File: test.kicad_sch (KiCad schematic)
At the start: 35 parts, among them IC1 USBLC6-2SC6, IC2 ESP32-S3-WROOM-1-N16, J1 PWM, J2 UART0, SW1 Reset, SW2 Button, U1 USB-TYPE-C-018, U2 ADC08351CILQX{slash}NOPB, U3 ADC08351CILQX{slash}NOPB

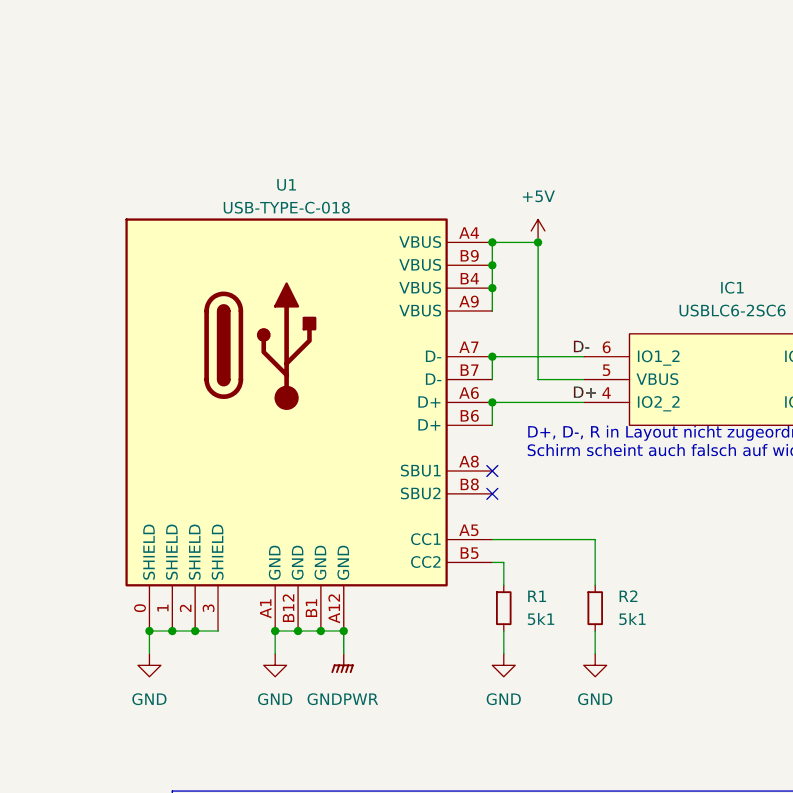
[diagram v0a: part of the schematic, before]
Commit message: new idear to arange gnd ref in layout
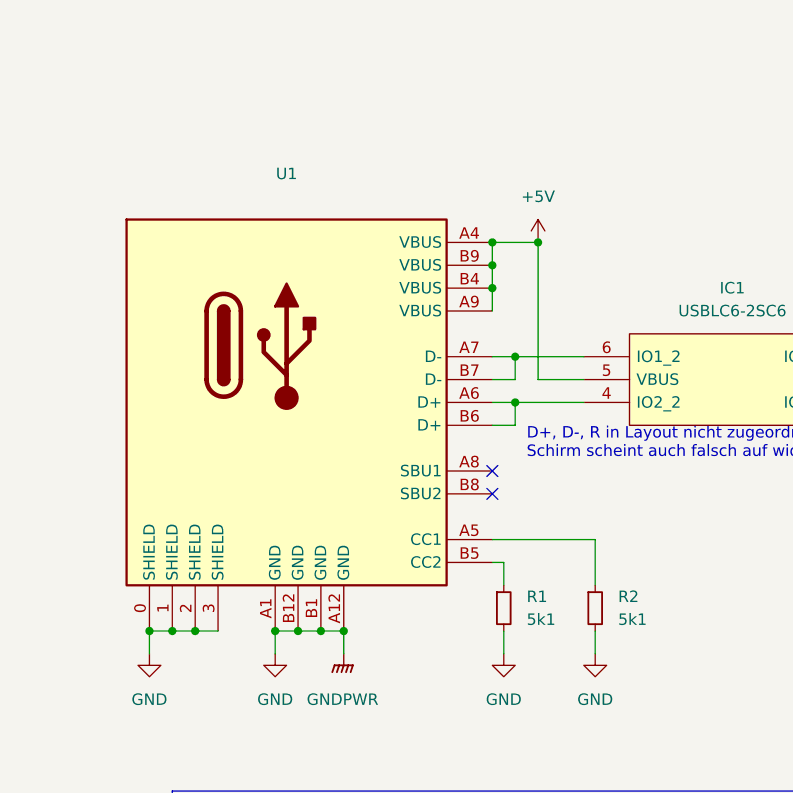
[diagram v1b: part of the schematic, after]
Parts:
- U1: value USB-TYPE-C-018 -> (none); footprint footprint:USB-C_SMD-TYPE-C-31-M-12 -> (none)
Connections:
- net D+: no longer names the net of IC1.4 (IO2_2), U1.A6 (D+), U1.B6 (D+)
- net D-: no longer names the net of IC1.6 (IO1_2), U1.A7 (D-), U1.B7 (D-)

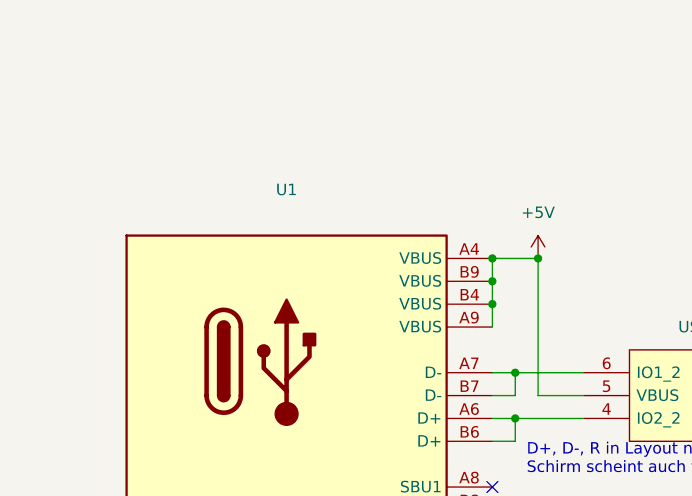
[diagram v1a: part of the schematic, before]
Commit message: added values for analog front end
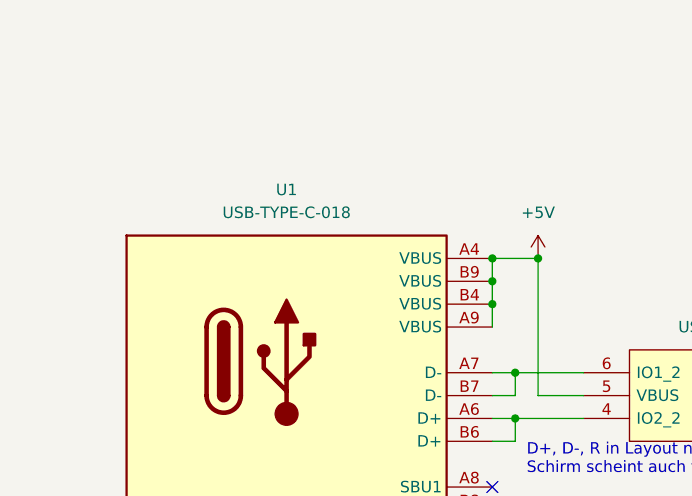
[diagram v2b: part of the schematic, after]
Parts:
- U1: value (none) -> USB-TYPE-C-018; footprint (none) -> project_library:USB-TYPE-C-018

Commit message: new adc
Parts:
- added IC?: AD9288BSTZ-40, project_library:QFP50P900X900X160-48N-AD9288, symbol project_library:AD9288BSTZ-40
- added U?: ESP32-WROOM-E, Espressif:ESP32-WROOM-32E, symbol Espressif:ESP32-WROOM-E
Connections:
- new net: U?.1 (GND), U?.15 (GND), U?.38 (GND)
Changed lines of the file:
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@@
     (pin "1")
+  )
+  (symbol (lib_id "Espressif:ESP32-WROOM-E") (at 415.29 59.69 0) (unit 1)
+    (in_bom yes) (on_board yes) (fields_autoplaced)
+    (property "Reference" "U?" (id 0) (at 415.29 21.59 0))
+    (property "Value" "ESP32-WROOM-E" (id 1) (at 415.29 24.13 0))
+    (property "Footprint" "Espressif:ESP32-WROOM-32E" (id 2) (at 415.29 97.79 0)
+      (effects (font (size 1.27 1.27)) hide)
+    )
+    (property "Datasheet" "https://www.espressif.com/sites/default/files/documentation/esp32-wroom-32e_esp32-wroom-32ue_datasheet_en.pdf" (id 3) (at 415.29 95.25 0)
+      (effects (font (size 1.27 1.27)) hide)
+    )
+    (pin "1")
+    (pin "10")
+    (pin "11")
+    (pin "12")
+    (pin "13")
+    (pin "14")
+    (pin "15")
+    (pin "16")
+    (pin "17")
+    (pin "18")
+    (pin "19")
+    (pin "2")
+    (pin "20")
+    (pin "21")
+    (pin "22")
+    (pin "23")
+    (pin "24")
+    (pin "25")
+    (pin "26")
+    (pin "27")
+    (pin "28")
+    (pin "29")
+    (pin "3")
+    (pin "30")
+    (pin "31")
+    (pin "32")
+    (pin "33")
+    (pin "34")
+    (pin "35")
+    (pin "36")
+    (pin "37")
+    (pin "38")
+    (pin "39")
+    (pin "4")
+    (pin "5")
+    (pin "6")
+    (pin "7")
+    (pin "8")
+    (pin "9")
   )
   (symbol (lib_id "project_library:Button") (at 111.76 38.1 90) (unit 1)
@@
     )
   )
+  (symbol (lib_id "project_library:AD9288BSTZ-40") (at 339.09 130.81 0) (unit 1)
+    (in_bom yes) (on_board yes) (fields_autoplaced)
+    (property "Reference" "IC?" (id 0) (at 386.08 124.2312 0))
+    (property "Value" "AD9288BSTZ-40" (id 1) (at 386.08 126.7712 0))
+    (property "Footprint" "project_library:QFP50P900X900X160-48N-AD9288" (id 2) (at 378.46 113.03 0)
+      (effects (font (size 1.27 1.27)) (justify left) hide)
+    )
+    (property "Datasheet" "http://www.analog.com/media/en/technical-documentation/data-sheets/AD9288.pdf" (id 3) (at 378.46 115.57 0)
+      (effects (font (size 1.27 1.27)) (justify left) hide)
+    )
+    (property "Description" "Analog Devices, AD9288BSTZ-40 Analog Devices AD9288BSTZ-40, 8 bit Parallel ADC, Dual Differential Input, 48-Pin LQFP" (id 4) (at 378.46 118.11 0)
+      (effects (font (size 1.27 1.27)) (justify left) hide)
+    )
+    (property "Height" "1.6" (id 5) (at 378.46 120.65 0)
+      (effects (font (size 1.27 1.27)) (justify left) hide)
+    )
+    (property "Mouser Part Number" "584-AD9288BSTZ-40" (id 6) (at 378.46 123.19 0)
+      (effects (font (size 1.27 1.27)) (justify left) hide)
+    )
+    (property "Mouser Price/Stock" "https://www.mouser.co.uk/ProductDetail/Analog-Devices/AD9288BSTZ-40?qs=%2FtpEQrCGXCxwGu1VSidU0Q%3D%3D" (id 7) (at 378.46 125.73 0)
+      (effects (font (size 1.27 1.27)) (justify left) hide)
+    )
+    (property "Manufacturer_Name" "Analog Devices" (id 8) (at 378.46 128.27 0)
+      (effects (font (size 1.27 1.27)) (justify left) hide)
+    )
+    (property "Manufacturer_Part_Number" "AD9288BSTZ-40" (id 9) (at 378.46 130.81 0)
+      (effects (font (size 1.27 1.27)) (justify left) hide)
+    )
+    (pin "1")
+    (pin "10")
+    (pin "11")
+    (pin "12")
+    (pin "13")
+    (pin "14")
+    (pin "15")
+    (pin "16")
+    (pin "17")
+    (pin "18")
+    (pin "19")
+    (pin "2")
+    (pin "20")
+    (pin "21")
+    (pin "22")
+    (pin "23")
+    (pin "24")
+    (pin "25")
+    (pin "26")
+    (pin "27")
+    (pin "28")
+    (pin "29")
+    (pin "3")
+    (pin "30")
+    (pin "31")
+    (pin "32")
+    (pin "33")
+    (pin "34")
+    (pin "35")
+    (pin "36")
+    (pin "37")
+    (pin "38")
+    (pin "39")
+    (pin "4")
+    (pin "40")
+    (pin "41")
+    (pin "42")
+    (pin "43")
+    (pin "44")
+    (pin "45")
+    (pin "46")
+    (pin "47")
+    (pin "48")
+    (pin "5")
+    (pin "6")
+    (pin "7")
+    (pin "8")
+    (pin "9")
+  )
   (symbol (lib_id "power:+3.3V") (at 247.65 50.8 0) (unit 1)
     (in_bom yes) (on_board yes) (fields_autoplaced)
@@
       (reference "IC10") (unit 1) (value "DAC5571IDBVR") (footprint "project_library:DAC5571IDBVR")
     )
+    (path "/f319d031-f112-4b08-a205-7d9414f5c3bf"
+      (reference "IC?") (unit 1) (value "AD9288BSTZ-40") (footprint "project_library:QFP50P900X900X160-48N-AD9288")
+    )
     (path "/ff062df5-8115-40ac-9e51-b96c9808f42d"
       (reference "J1") (unit 1) (value "PWM") (footprint "project_library:725996-2")
@@
       (reference "U10") (unit 3) (value "MCP6022T-I_SN") (footprint "project_library:MCP6022T-I_SN")
     )
-  )
+    (path "/d6fb04dc-8dd4-47e8-aa6e-91850d9215a1"
+      (reference "U?") (unit 1) (value "ESP32-WROOM-E") (footprint "Espressif:ESP32-WROOM-32E")
+    )
+  )

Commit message: changed adc and esp chip
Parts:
- removed C10, C13, C2, C5: 10u, Capacitor_SMD:C_0805_2012Metric_Pad1.18x1.45mm_HandSolder, symbol Device:C_Small
- removed C11, C12, C3, C4, C9: 0.1u, Capacitor_SMD:C_0805_2012Metric_Pad1.18x1.45mm_HandSolder, symbol Device:C_Small
- removed R3: 5k1, Resistor_SMD:R_0805_2012Metric_Pad1.20x1.40mm_HandSolder, symbol Device:R_Small
- removed SW2: Button, project_library:SW_TS-1187A-B-A-B, symbol project_library:Button
- removed U2, U3: ADC08351CILQX/NOPB, project_library:ADC08351CILQX, symbol project_library:ADC08351CILQX{brace}slash}NOPB
- added C? (x9): 0.1u, Capacitor_SMD:C_0805_2012Metric_Pad1.18x1.45mm_HandSolder, symbol Device:C_Small
- added C?: (no value), symbol Device:C_Small
- added Q?: (no value), symbol project_library:SS8050-G
- added Q?: SS8050-G, SOT95P240X115-3N, symbol project_library:SS8050-G
- added R? (x3): (no value), symbol Device:R_Small
- added R? (x2): 10k, Resistor_SMD:R_0805_2012Metric_Pad1.20x1.40mm_HandSolder, symbol Device:R_Small
- added R?: (no value), Resistor_SMD:R_0805_2012Metric_Pad1.20x1.40mm_HandSolder, symbol Device:R_Small
- added SW?: (no value), project_library:SW_TS-1187A-B-A-B, symbol project_library:Button
- added U?: (no value), symbol Interface_USB:CP2102N-Axx-xQFN28
- C6: value 1u -> (none); footprint Capacitor_SMD:C_0805_2012Metric_Pad1.18x1.45mm_HandSolder -> (none)
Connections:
- net +3.3VA: now also IC?.30 (VD_2), IC?.31 (VD_3), IC?.48 (VD_4), C?.1, C?.1
- net +3V3: now also IC?.15 (VDD_1), IC?.28 (VDD_2), IC?.33 (VDD_3), IC?.46 (VDD_4), IC?.8 (S1), IC?.9 (S2), C?.1, C?.1, C?.1, C?.1, C?.1, R?.1, U?.6 (VDD), U?.7 (VREGIN); no longer C1.1
- net +5V: now also R?.1
- net Analog_Out_CH1: now also IC?.2 (AINA)
- net Analog_Out_CH2: now also IC?.11 (AINB)
- net CH1_D0: now also IC?.37 (D0A)
- net CH1_D1: now also IC?.38 (D1A)
- net CH1_D2: now also IC?.39 (D2A)
- net CH1_D3: now also IC?.40 (D3A)
- net CH1_D4: now also IC?.41 (D4A)
- net CH1_D5: now also IC?.42 (D5A)
- net CH1_D6: now also IC?.43 (D6A)
- net CH1_D7: now also IC?.44 (D7A_(MSB))
- net CH2_D0: now also IC?.24 (D0B)
- net CH2_D1: now also IC?.23 (D1B)
- net CH2_D2: now also IC?.22 (D2B)
- net CH2_D3: now also IC?.21 (D3B)
- net CH2_D4: now also IC?.20 (D4B)
- net CH2_D5: now also IC?.19 (D5B)
- net CH2_D6: now also IC?.18 (D6B)
- net CH2_D7: now also IC?.17 ((MSB)_D7B)
- net ENABLE: now also Q?.3; no longer IC2.3 (EN)
- net GND: now also IC?.16 (GND_3), IC?.27 (GND_4), IC?.34 (GND_7), IC?.45 (GND_8), C?.2, C?.2, C?.2, C?.2, C?.2, C?.2, R?.1, R?.2, SW?.A, SW?.B, U?.29 (GND), U?.3 (GND); no longer C1.2
- net I2S_CLK: now also IC?.14 (ENCB), IC?.47 (ENCA)
- net USB_D+: now also U?.4 (D+); no longer IC1.3 (IO2_1), IC2.14 (IO20)
- net USB_D-: now also U?.5 (D-); no longer IC1.1 (IO1_1), IC2.13 (IO19)
- net at U?.34 (U0RXD/GPIO3): now also U?.26 (TXD)
- net at U?.35 (U0TXD/GPIO1): now also U?.25 (RXD)
- net GNDA: now reaches IC?.1 (GND_1)
- net GNDA: now also IC?.29 (GND_5), IC?.32 (GND_6), C?.2, C?.2, C?.2
- net at IC?.12 (GND_2): now also C?.1
- net at IC?.13 (VD_1): now also C?.2
- new net: Q?.1, R?.2 (x2)
- new net: R?.1, U?.11 (~{SUSPEND})
- new net: R?.2, R?.2, U?.8 (VBUS)
- new net: R?.2, U?.9 (~{RST})
- new net DTR: Q?.2, R?.1, U?.28 (~{DTR})
- new net IO0: C?.1, Q?.3, SW?.C, SW?.D
- new net RTS: Q?.2, R?.1, U?.24 (~{RTS})
- no-connect marks 15 -> 24
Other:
- moved on the sheet: C1, C6, C7, C8, SW1

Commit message: updated circuit
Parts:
- removed C1: 0.1u, Capacitor_SMD:C_0805_2012Metric_Pad1.18x1.45mm_HandSolder, symbol Device:C_Small
- removed IC2: ESP32-S3-WROOM-1-N16, project_library:ESP32-S3-WROOM-1, symbol project_library:ESP32-S3-WROOM-1-N16
- removed J2: UART0, Connector_PinHeader_2.54mm:PinHeader_1x04_P2.54mm_Vertical, symbol Connector:Conn_01x04_Male
- removed R4, R5: 6k8, Resistor_SMD:R_0805_2012Metric_Pad1.20x1.40mm_HandSolder, symbol Device:R_Small
- removed R6, R7: 470, Resistor_SMD:R_0805_2012Metric_Pad1.20x1.40mm_HandSolder, symbol Device:R_Small
- removed R8: 1k5, Resistor_SMD:R_0805_2012Metric_Pad1.20x1.40mm_HandSolder, symbol Device:R_Small
- added IC5: TCA9534APWR, project_library:SOP65P640X120-16N, symbol project_library:TCA9534APWR
- added R15: 1k5, Resistor_SMD:R_0805_2012Metric_Pad1.20x1.40mm_HandSolder, symbol Device:R_Small
- added R16, R17: 6k8, Resistor_SMD:R_0805_2012Metric_Pad1.20x1.40mm_HandSolder, symbol Device:R_Small
- added TP4: GNDREF, TestPoint:TestPoint_Keystone_5000-5004_Miniature, symbol Connector:TestPoint
- C10, C11, C12, C2, C3, C5, C9: renamed from C?; footprint Capacitor_SMD:C_0805_2012Metric_Pad1.18x1.45mm_HandSolder -> Capacitor_SMD:C_0603_1608Metric_Pad1.08x0.95mm_HandSolder
- C13: renamed from C?; value (none) -> 0.1u; footprint (none) -> Capacitor_SMD:C_0603_1608Metric_Pad1.08x0.95mm_HandSolder
- C6: value (none) -> 0.1u; footprint (none) -> Capacitor_SMD:C_0805_2012Metric_Pad1.18x1.45mm_HandSolder
- Q1: renamed from Q?; footprint SOT95P240X115-3N -> project_library:SOT95P240X115-3N
- Q2: renamed from Q?; value (none) -> SS8050-G; footprint (none) -> project_library:SOT95P240X115-3N
- R3: renamed from R?; value (none) -> 22.1k; footprint (none) -> Resistor_SMD:R_0805_2012Metric_Pad1.20x1.40mm_HandSolder
- R4: renamed from R?; value (none) -> 47.5k
- R5: renamed from R?; value (none) -> 2k; footprint (none) -> Resistor_SMD:R_0805_2012Metric_Pad1.20x1.40mm_HandSolder
- R6: renamed from R?; value (none) -> 10k; footprint (none) -> Resistor_SMD:R_0805_2012Metric_Pad1.20x1.40mm_HandSolder
- SW2: renamed from SW?; value (none) -> Button
- U2: renamed from U?; value (none) -> CP2102N-A02-GQFN28; footprint (none) -> Package_DFN_QFN:QFN-28-1EP_5x5mm_P0.5mm_EP3.35x3.35mm
- gave numbers to parts that had none: 6
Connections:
- net +3V3: now also IC2.4 (DFS), U3.2 (3V3), IC5.16 (VCC), R16.2, R17.2
- net CH1_AC_Sel: now also IC5.6 (P2)
- net CH1_D0: now also U3.23 (MTDO/GPIO15/ADC2_CH3)
- net CH1_D1: now also U3.14 (MTDI/GPIO12/ADC2_CH5)
- net CH1_D2: now also U3.9 (32K_XN/GPIO33/ADC1_CH5)
- net CH1_D3: now also U3.8 (32K_XP/GPIO32/ADC1_CH4)
- net CH1_D4: now also U3.7 (GPIO35/ADC1_CH7)
- net CH1_D5: now also U3.6 (GPIO34/ADC1_CH6)
- net CH1_D6: now also U3.5 (SENSOR_VN/GPIO39/ADC1_CH3)
- net CH1_D7: now also U3.4 (SENSOR_VP/GPIO36/ADC1_CH0)
- net CH2_AC_Sel: now also IC5.9 (P4)
- net CH2_D0: now also U3.37 (GPIO23)
- net CH2_D1: now also U3.31 (GPIO19)
- net CH2_D2: now also U3.30 (GPIO18)
- net CH2_D3: now also U3.28 (GPIO17)
- net CH2_D4: now also U3.27 (GPIO16)
- net CH2_D5: now also U3.29 (GPIO5)
- net CH2_D6: now also U3.26 (ADC2_CH0/GPIO4)
- net CH2_D7: now also U3.24 (ADC2_CH2/GPIO2)
- net CS_Gain_CH1: now also IC5.7 (P3)
- net CS_Gain_CH2: now also IC5.10 (P5)
- net Charging: now also IC5.11 (P6)
- net ENABLE: now also U3.3 (EN/CHIP_PU)
- net GND: now also U3.1 (GND), U3.15 (GND), U3.38 (GND), U3.39 (GND_THERMAL), IC5.1 (A0), IC5.2 (A1), IC5.3 (A2), IC5.8 (GND)
- net I2S_CLK: now also U3.12 (ADC2_CH7/GPIO27)
- net IO0: now also U3.25 (GPIO0/BOOT/ADC2_CH1)
- net MOSI: now also U3.16 (MTCK/GPIO13/ADC2_CH4)
- net RX: now also U2.25 (RXD), U3.34 (U0RXD/GPIO3)
- net SCLK_SPI: now also U3.13 (MTMS/GPIO14/ADC2_CH6)
- net SCL_I2C: now also U3.36 (GPIO22), IC5.14 (SCL), R16.1
- net SDA: now also U3.33 (GPIO21), IC5.15 (SDA), R17.1
- net Status_PWM: now also IC5.12 (P7), R15.2
- net TX: now also U2.26 (TXD), U3.35 (U0TXD/GPIO1)
- net Trigger_CH1: now also IC5.4 (P0)
- net Trigger_CH2: now also IC5.5 (P1)
- net USB_D+: now also IC1.3 (IO2_1)
- net USB_D-: now also IC1.1 (IO1_1)
- net at D1.2 (A): now also R15.1
- net Offset_CH1: now reaches U3.10 (DAC_1/ADC2_CH8/GPIO25)
- net Offset_CH2: now reaches U3.11 (DAC_2/ADC2_CH9/GPIO26)
- net GNDREF: now reaches IC2.5 (REFINA)
- net GNDREF: now also IC2.6 (REFOUT), IC2.7 (REFINB), TP4.1
- no-connect marks 24 -> 22
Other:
- moved on the sheet: C18, C4, C6, C7, C8, IC1, Q1, Q2, R1, R2, R3, R4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

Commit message: routing
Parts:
- removed C4, C6: 0.1u, Capacitor_SMD:C_0805_2012Metric_Pad1.18x1.45mm_HandSolder, symbol Device:C_Small
- removed D1: Status, LED_SMD:LED_0805_2012Metric_Pad1.15x1.40mm_HandSolder, symbol Device:LED_Small
- removed IC1: USBLC6-2SC6, project_library:USBLC6-2SC6, symbol project_library:USBLC6-2SC6
- removed IC5: TCA9534APWR, project_library:SOP65P640X120-16N, symbol project_library:TCA9534APWR
- removed J1: PWM, project_library:725996-2, symbol Connector:Conn_01x02_Male
- removed Q1, Q2: SS8050-G, project_library:SOT95P240X115-3N, symbol project_library:SS8050-G
- removed R1, R2: 5k1, Resistor_SMD:R_0805_2012Metric_Pad1.20x1.40mm_HandSolder, symbol Device:R_Small
- removed R15: 1k5, Resistor_SMD:R_0805_2012Metric_Pad1.20x1.40mm_HandSolder, symbol Device:R_Small
- removed R3: 22.1k, Resistor_SMD:R_0805_2012Metric_Pad1.20x1.40mm_HandSolder, symbol Device:R_Small
- removed R4: 47.5k, Resistor_SMD:R_0805_2012Metric_Pad1.20x1.40mm_HandSolder, symbol Device:R_Small
- removed R5: 2k, Resistor_SMD:R_0805_2012Metric_Pad1.20x1.40mm_HandSolder, symbol Device:R_Small
- removed R6, R7, R8: 10k, Resistor_SMD:R_0805_2012Metric_Pad1.20x1.40mm_HandSolder, symbol Device:R_Small
- removed SW1: Reset, project_library:SW_TS-1187A-B-A-B, symbol project_library:Button
- removed SW2: Button, project_library:SW_TS-1187A-B-A-B, symbol project_library:Button
- removed U1: USB-TYPE-C-018, project_library:USB-TYPE-C-018, symbol project_library:USB-TYPE-C-018
- removed U2: CP2102N-A02-GQFN28, Package_DFN_QFN:QFN-28-1EP_5x5mm_P0.5mm_EP3.35x3.35mm, symbol Interface_USB:CP2102N-Axx-xQFN28
- C18, C8: value 0.1u -> (none); footprint Capacitor_SMD:C_0805_2012Metric_Pad1.18x1.45mm_HandSolder -> (none)
- C7: value 22u -> (none); footprint Capacitor_SMD:C_0805_2012Metric_Pad1.18x1.45mm_HandSolder -> (none)
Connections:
- net MOSI is gone; now on net Trigger_CH2: U3.16 (MTCK/GPIO13/ADC2_CH4)
- net SCLK_SPI is gone; now on net CH1_D6: U3.13 (MTMS/GPIO14/ADC2_CH6)
- net +3.3VA: now also C3.1
- net CH1_D0: now also U3.4 (SENSOR_VP/GPIO36/ADC1_CH0); no longer U3.23 (MTDO/GPIO15/ADC2_CH3)
- net CH1_D1: now also U3.5 (SENSOR_VN/GPIO39/ADC1_CH3); no longer U3.14 (MTDI/GPIO12/ADC2_CH5)
- net CH1_D2: now also U3.6 (GPIO34/ADC1_CH6); no longer U3.9 (32K_XN/GPIO33/ADC1_CH5)
- net CH1_D3: now also U3.7 (GPIO35/ADC1_CH7); no longer U3.8 (32K_XP/GPIO32/ADC1_CH4)
- net CH1_D4: now also U3.8 (32K_XP/GPIO32/ADC1_CH4); no longer U3.7 (GPIO35/ADC1_CH7)
- net CH1_D5: now also U3.9 (32K_XN/GPIO33/ADC1_CH5); no longer U3.6 (GPIO34/ADC1_CH6)
- net CH1_D6: no longer U3.5 (SENSOR_VN/GPIO39/ADC1_CH3)
- net CH1_D7: now also U3.14 (MTDI/GPIO12/ADC2_CH5); no longer U3.4 (SENSOR_VP/GPIO36/ADC1_CH0)
- net CH2_D0: now also U3.24 (ADC2_CH2/GPIO2); no longer U3.37 (GPIO23)
- net CH2_D1: now also U3.26 (ADC2_CH0/GPIO4); no longer U3.31 (GPIO19)
- net CH2_D2: now also U3.29 (GPIO5); no longer U3.30 (GPIO18)
- net CH2_D3: now also U3.27 (GPIO16); no longer U3.28 (GPIO17)
- net CH2_D4: now also U3.28 (GPIO17); no longer U3.27 (GPIO16)
- net CH2_D5: now also U3.30 (GPIO18); no longer U3.29 (GPIO5)
- net CH2_D6: now also U3.31 (GPIO19); no longer U3.26 (ADC2_CH0/GPIO4)
- net CH2_D7: now also U3.37 (GPIO23); no longer U3.24 (ADC2_CH2/GPIO2)
- net GND: no longer C18.2
- net GNDA: now also IC2.10 (~{AINB}), IC2.3 (~{AINA})
- net IO0: no longer C18.1
- net Trigger_CH1: now also U3.23 (MTDO/GPIO15/ADC2_CH3)
- net at C12.1, IC2.12 (GND_2): now also C18.1
- net at C12.2, IC2.13 (VD_1): now also C18.2
- no-connect marks 22 -> 4
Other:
- added sheet USB and GPIO Expander (USB_GPIO.kicad_sch)
- note removed: "D+, D-, R in Layout nicht zugeordnet Schirm scheint auch falsch auf widerstand zu gehen"
- moved on the sheet: C10, C11, C12, C13, C2, C3, C5, C9, IC2, R16, R17, TP4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
